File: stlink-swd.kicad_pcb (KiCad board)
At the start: 2 copper layers, 35.6 x 15.2 mm, 18 parts, among them J1 Conn_02x03_Odd_Even, J2 Ribbon IDC DIP, J3 SWD-RA, J4 Conn_01x02, SW1 KS-00Q-02

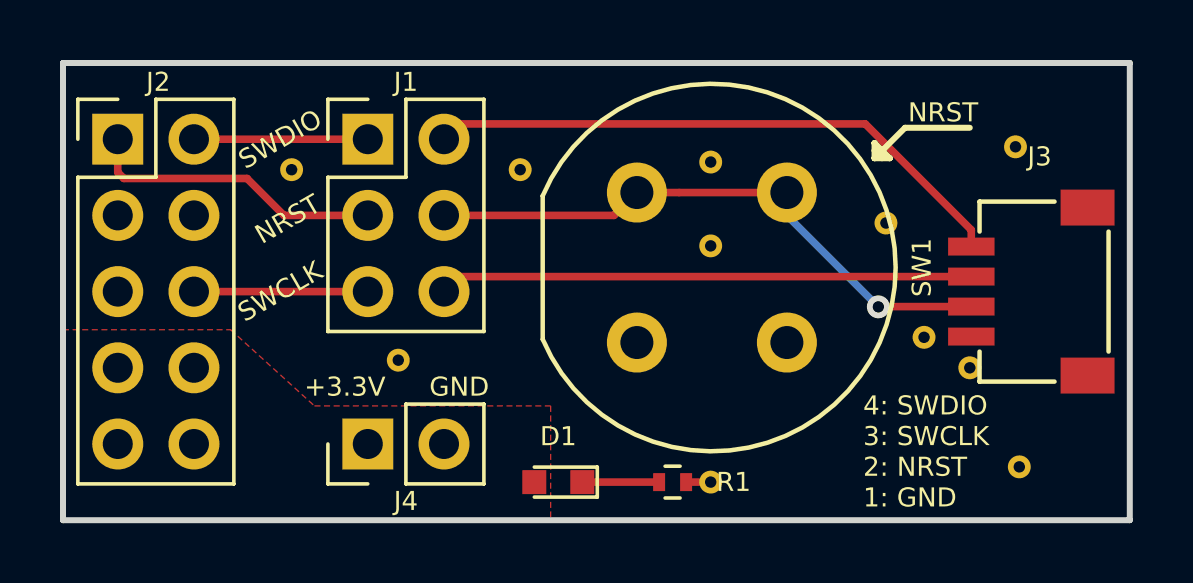
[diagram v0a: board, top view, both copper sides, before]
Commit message: Added part numbers and rounded PCB edges
Also deleted some temporary BOM files that got checked in.
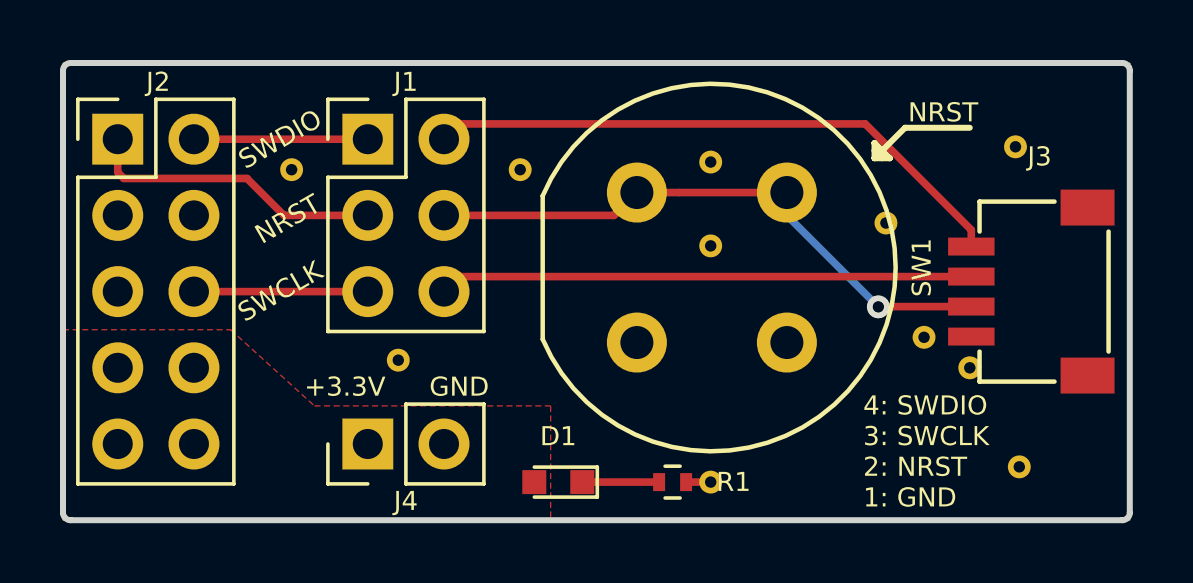
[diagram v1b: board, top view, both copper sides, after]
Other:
- outline, holes or cut-outs redrawn
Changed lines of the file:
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@@
   (general
     (thickness 1.6)
-    (drawings 23)
+    (drawings 27)
     (tracks 24)
     (zones 0)
@@
     (trace_min 0.1524)
     (segment_width 0.2)
-    (edge_width 0.15)
+    (edge_width 0.2)
     (via_size 0.762)
     (via_drill 0.381)
@@
       (net 12 GND) (zone_connect 2))
   )
+  (gr_arc (start 162.306 105.156) (end 162.306 105.41) (angle -90) (layer Edge.Cuts) (width 0.2))
+  (gr_arc (start 127.254 105.156) (end 127 105.156) (angle -90) (layer Edge.Cuts) (width 0.2))
+  (gr_arc (start 127.254 90.424) (end 127.254 90.17) (angle -90) (layer Edge.Cuts) (width 0.2))
+  (gr_arc (start 162.306 90.424) (end 162.56 90.424) (angle -90) (layer Edge.Cuts) (width 0.2))
   (gr_text "Rev A\n2019" (at 162.052 95.504) (layer B.SilkS)
     (effects (font (size 0.635 0.635) (thickness 0.127)) (justify left mirror))
@@
     (arrow2b (pts (xy 127 86.36) (xy 128.126504 85.773579)))
   )
-  (gr_line (start 127 105.41) (end 127 90.17) (layer Edge.Cuts) (width 0.2))
-  (gr_line (start 162.56 105.41) (end 127 105.41) (layer Edge.Cuts) (width 0.2))
-  (gr_line (start 162.56 90.17) (end 162.56 105.41) (layer Edge.Cuts) (width 0.2))
-  (gr_line (start 127 90.17) (end 162.56 90.17) (layer Edge.Cuts) (width 0.2))
+  (gr_line (start 127 105.156) (end 127 90.424) (layer Edge.Cuts) (width 0.2))
+  (gr_line (start 162.306 105.41) (end 127.254 105.41) (layer Edge.Cuts) (width 0.2))
+  (gr_line (start 162.56 90.424) (end 162.56 105.156) (layer Edge.Cuts) (width 0.2))
+  (gr_line (start 127.254 90.17) (end 162.306 90.17) (layer Edge.Cuts) (width 0.2))
   (segment (start 146.87 104.14) (end 144.31 104.14) (width 0.254) (layer F.Cu) (net 1))
   (segment (start 129.03 94.018999) (end 133.134999 94.018999) (width 0.254) (layer F.Cu) (net 3))
